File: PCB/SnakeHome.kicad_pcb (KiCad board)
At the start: 2 copper layers, 26.7 x 55.9 mm, 7 parts, among them J1 Raspberry_Pi_4, U1 Temp&Humidity_R1, U2 PIR_motion_Kitchen, U4 PIR_motion_Toilet, U5 Temp&Humidity_R2, U6 Temp&Humidity_R3, U7 Temp&Humidity_Kitchen

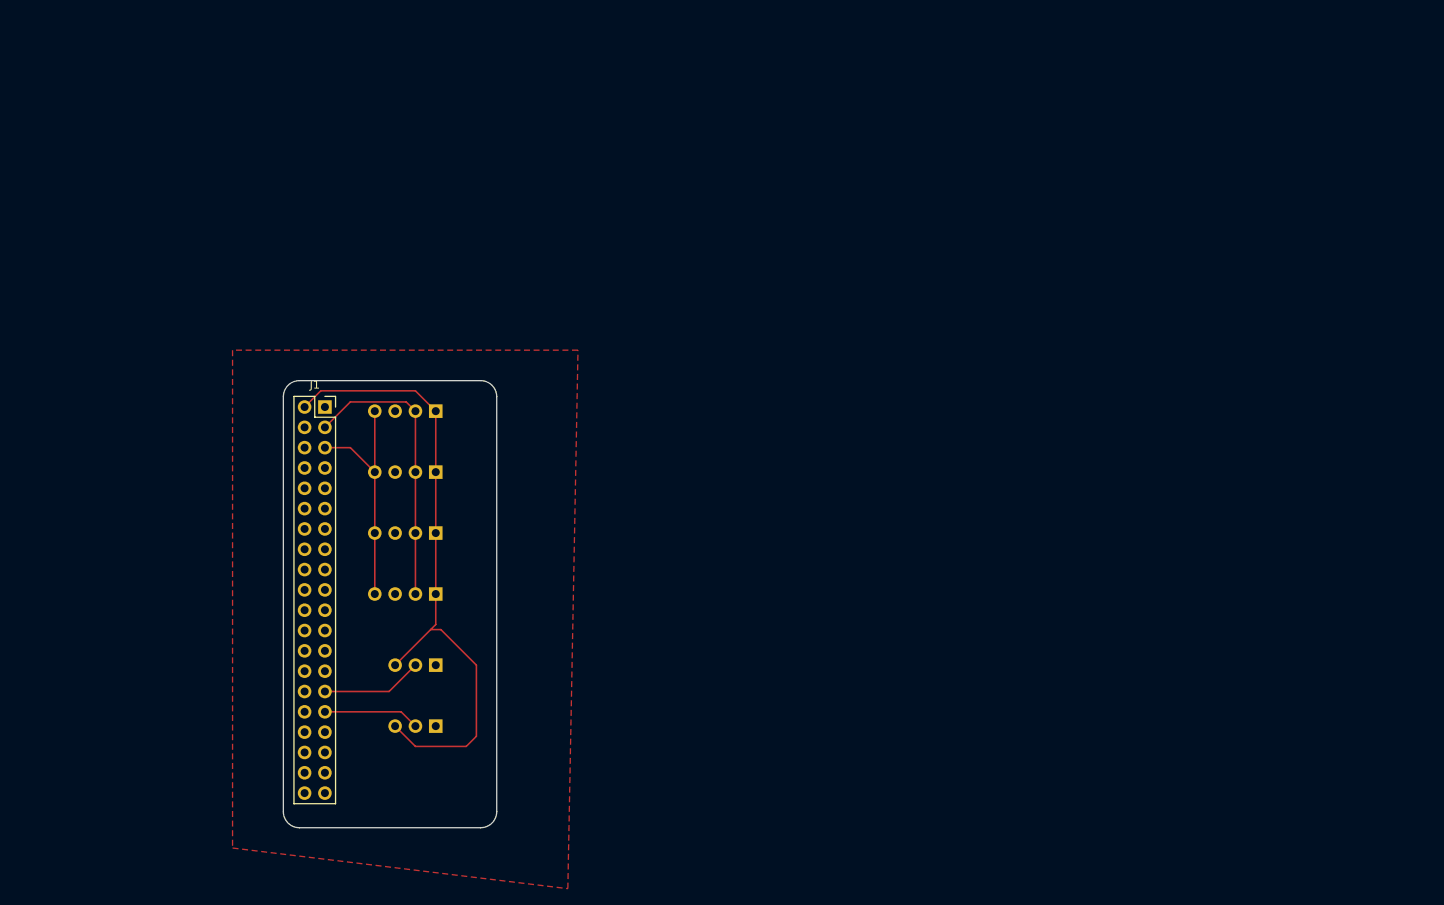
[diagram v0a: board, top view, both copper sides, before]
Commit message: choosed smd Rs and placed the components on the PCB
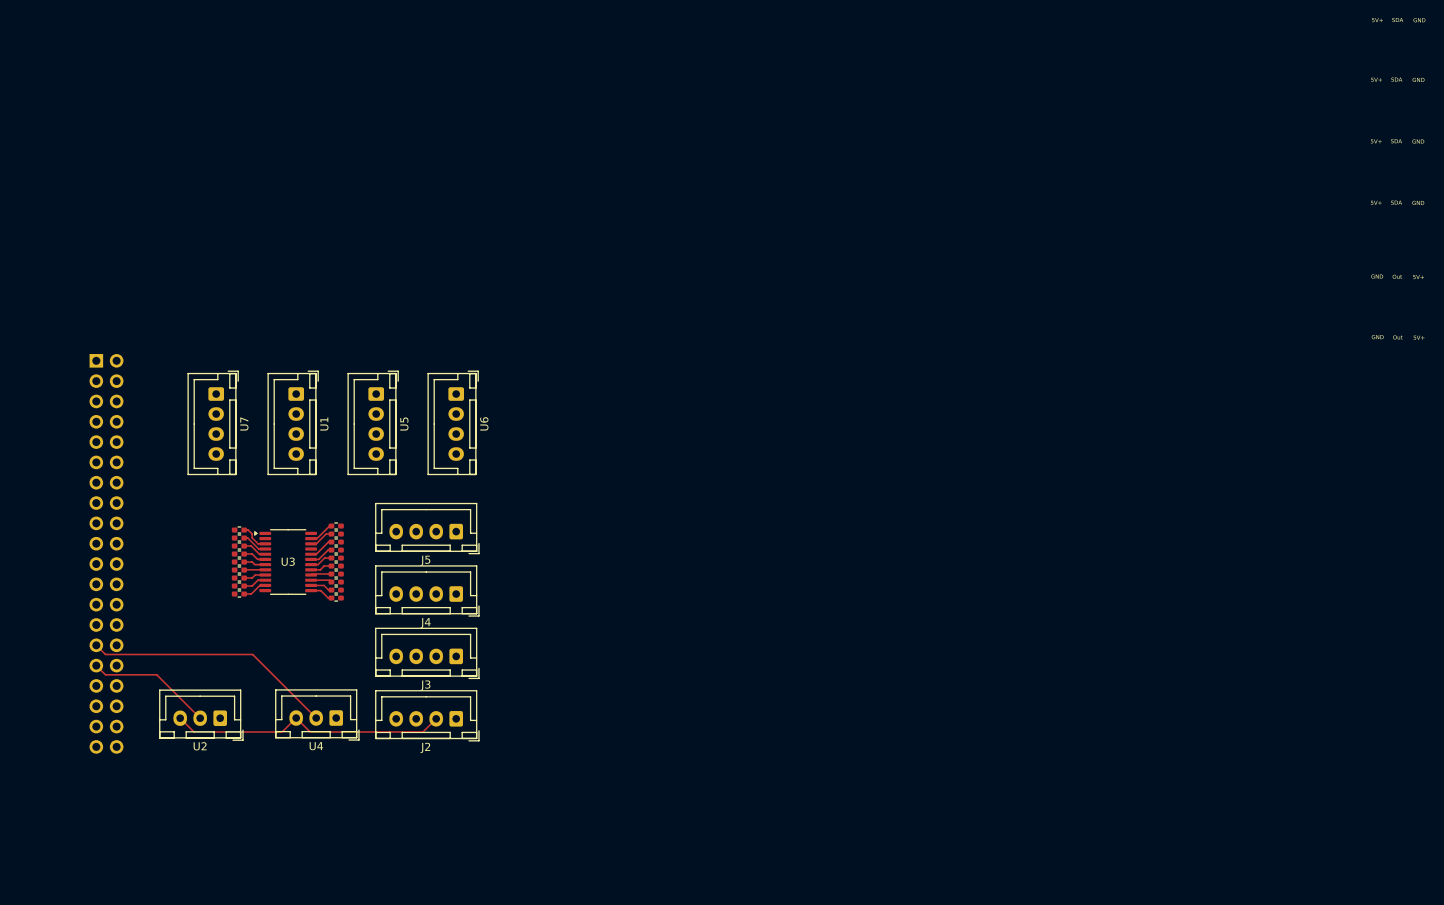
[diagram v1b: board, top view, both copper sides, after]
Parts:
- added J2: Conn_01x04_Pin, Connector_JST:JST_XH_B4B-XH-A_1x04_P2.50mm_Vertical, F.Cu at (143.5, 110.8)
- added J3: Conn_01x04_Pin, Connector_JST:JST_XH_B4B-XH-A_1x04_P2.50mm_Vertical, F.Cu at (143.5, 103.0)
- added J4: Conn_01x04_Pin, Connector_JST:JST_XH_B4B-XH-A_1x04_P2.50mm_Vertical, F.Cu at (143.5, 95.2)
- added J5: Conn_01x04_Pin, Connector_JST:JST_XH_B4B-XH-A_1x04_P2.50mm_Vertical, F.Cu at (143.5, 87.5)
- added R1: R, Resistor_SMD:R_0402_1005Metric_Pad0.72x0.64mm_HandSolder, F.Cu at (116.4, 87.2)
- added R10: R, Resistor_SMD:R_0402_1005Metric_Pad0.72x0.64mm_HandSolder, F.Cu at (128.5, 94.8)
- added R11: R, Resistor_SMD:R_0402_1005Metric_Pad0.72x0.64mm_HandSolder, F.Cu at (128.5, 90.8)
- added R12: R, Resistor_SMD:R_0402_1005Metric_Pad0.72x0.64mm_HandSolder, F.Cu at (128.5, 95.8)
- added R13: R, Resistor_SMD:R_0402_1005Metric_Pad0.72x0.64mm_HandSolder, F.Cu at (128.5, 91.8)
- added R14: R, Resistor_SMD:R_0402_1005Metric_Pad0.72x0.64mm_HandSolder, F.Cu at (128.5, 92.8)
- added R15: R, Resistor_SMD:R_0402_1005Metric_Pad0.72x0.64mm_HandSolder, F.Cu at (128.5, 88.8)
- added R16: R, Resistor_SMD:R_0402_1005Metric_Pad0.72x0.64mm_HandSolder, F.Cu at (128.5, 93.8)
- added R17: R, Resistor_SMD:R_0402_1005Metric_Pad0.72x0.64mm_HandSolder, F.Cu at (128.5, 89.8)
- added R18: R, Resistor_SMD:R_0402_1005Metric_Pad0.72x0.64mm_HandSolder, F.Cu at (128.5, 87.8)
- added R19: R, Resistor_SMD:R_0402_1005Metric_Pad0.72x0.64mm_HandSolder, F.Cu at (128.5, 86.8)
- added R2: R, Resistor_SMD:R_0402_1005Metric_Pad0.72x0.64mm_HandSolder, F.Cu at (116.4, 89.2)
- added R3: R, Resistor_SMD:R_0402_1005Metric_Pad0.72x0.64mm_HandSolder, F.Cu at (116.4, 88.2)
- added R4: R, Resistor_SMD:R_0402_1005Metric_Pad0.72x0.64mm_HandSolder, F.Cu at (116.4, 91.2)
- added R5: R, Resistor_SMD:R_0402_1005Metric_Pad0.72x0.64mm_HandSolder, F.Cu at (116.4, 90.2)
- added R6: R, Resistor_SMD:R_0402_1005Metric_Pad0.72x0.64mm_HandSolder, F.Cu at (116.4, 93.2)
- added R7: R, Resistor_SMD:R_0402_1005Metric_Pad0.72x0.64mm_HandSolder, F.Cu at (116.4, 92.2)
- added R8: R, Resistor_SMD:R_0402_1005Metric_Pad0.72x0.64mm_HandSolder, F.Cu at (116.4, 95.2)
- added R9: R, Resistor_SMD:R_0402_1005Metric_Pad0.72x0.64mm_HandSolder, F.Cu at (116.4, 94.2)
- added U3: TCA9548APWR, Package_SO:TSSOP-24_4.4x7.8mm_P0.65mm, F.Cu at (122.5, 91.2)
- J1: moved to B.Cu
- U1, U5, U6, U7: footprint Connector_PinHeader_2.54mm:PinHeader_1x04_P2.54mm_Vertical -> Connector_JST:JST_XH_B4B-XH-A_1x04_P2.50mm_Vertical; moved to F.Cu
- U2, U4: footprint Connector_PinHeader_2.54mm:PinHeader_1x03_P2.54mm_Vertical -> Connector_JST:JST_XH_B3B-XH-A_1x03_P2.50mm_Vertical; moved to F.Cu
- moved U1 30.5 mm to (123.5, 70.2), turned to -90 degrees
- moved J1 29.2 mm to (98.5, 66.1), turned to 180 degrees
- moved U7 27.5 mm to (113.5, 70.2), turned to -90 degrees
- moved U2 27.0 mm to (114.0, 110.8), turned to 180 degrees
- moved U5 18.9 mm to (133.5, 70.2), turned to -90 degrees
- moved U4 14.1 mm to (128.5, 110.8), turned to 180 degrees
- moved U6 10.1 mm to (143.5, 70.2), turned to -90 degrees
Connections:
- J1 pad 3: SDA_temp -> SDA_Bus
- J1 pad 5: SCL_temp -> SCL_Bus
- U1 pad 2: SDA_temp -> SDA_R1
- U1 pad 4: SCL_temp -> SCL_R1
- U5 pad 2: SDA_temp -> SDA_R2
- U5 pad 4: SCL_temp -> SCL_R2
- U6 pad 2: SDA_temp -> SDA_R3
- U6 pad 4: SCL_temp -> SCL_R3
- U7 pad 2: SDA_temp -> SDA_Ki
- U7 pad 4: SCL_temp -> SCL_Ki
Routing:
- net +5V: track 80.3 -> 34.8 mm
- net SDA_temp: track 36.0 -> 0.00 mm
- net SCL_temp: track 30.4 -> 0.00 mm
- net motion_out2: track 12.7 -> 31.3 mm
- net motion_out: track 12.1 -> 15.7 mm
- net Net-(U3-~{RESET}): track 0.00 -> 3.64 mm
- net SCL_R1: track 0.00 -> 3.21 mm
- net SDA_Bus: track 0.00 -> 3.19 mm
- net SDA_4: track 0.00 -> 3.17 mm
- net SDA_Ki: track 0.00 -> 3.08 mm
- net SDA_R1: track 0.00 -> 3.06 mm
- net SCL_Bus: track 0.00 -> 3.05 mm
- net SCL_4: track 0.00 -> 3.03 mm
- net SCL_Ki: track 0.00 -> 2.94 mm
- net SCL_1: track 0.00 -> 2.92 mm
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- removed copper zone on F.Cu, net GND
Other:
- board outline removed
- board text removed: "SCL"

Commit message: Traced all the Components, used two back layer traces 😭
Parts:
- moved U6 30.0 mm to (113.5, 70.2)
- moved J2 15.6 mm to (143.5, 95.2)
- moved J4 15.6 mm to (143.5, 110.8)
- moved U1 10.0 mm to (133.5, 70.2)
- moved U5 10.0 mm to (143.5, 70.2)
- moved U7 10.0 mm to (123.5, 70.2)
- moved R10 0.25 mm to (128.5, 94.5)
- moved R11 0.25 mm to (128.5, 90.5)
- moved R12 0.25 mm to (128.5, 95.5)
- moved R13 0.25 mm to (128.5, 91.5)
- moved R14 0.25 mm to (128.5, 92.5)
- moved R15 0.25 mm to (128.5, 88.5)
- moved R16 0.25 mm to (128.5, 93.5)
- moved R17 0.25 mm to (128.5, 89.5)
- moved R18 0.25 mm to (128.5, 87.5)
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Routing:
- net +5V: track 34.8 -> 238.1 mm
- net SCL_Bus: track 3.05 -> 92.6 mm
- net SDA_Bus: track 3.19 -> 91.8 mm
- net SCL_Ki: track 2.94 -> 55.8 mm
- net SCL_R2: track 2.92 -> 45.2 mm
- net SDA_R3: track 2.79 -> 42.6 mm
- net SCL_R3: track 2.65 -> 37.8 mm
- net SDA_R2: track 2.77 -> 36.2 mm
- net SDA_Ki: track 3.08 -> 33.3 mm
- net SDA_R1: track 3.06 -> 32.1 mm
- net SCL_3: track 2.74 -> 30.3 mm
- net SDA_3: track 2.88 -> 29.7 mm
- net SCL_4: track 3.03 -> 29.4 mm, vias 0 -> 1
- net SDA_4: track 3.17 -> 25.4 mm, vias 0 -> 1
- net SCL_2: track 2.63 -> 24.0 mm
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
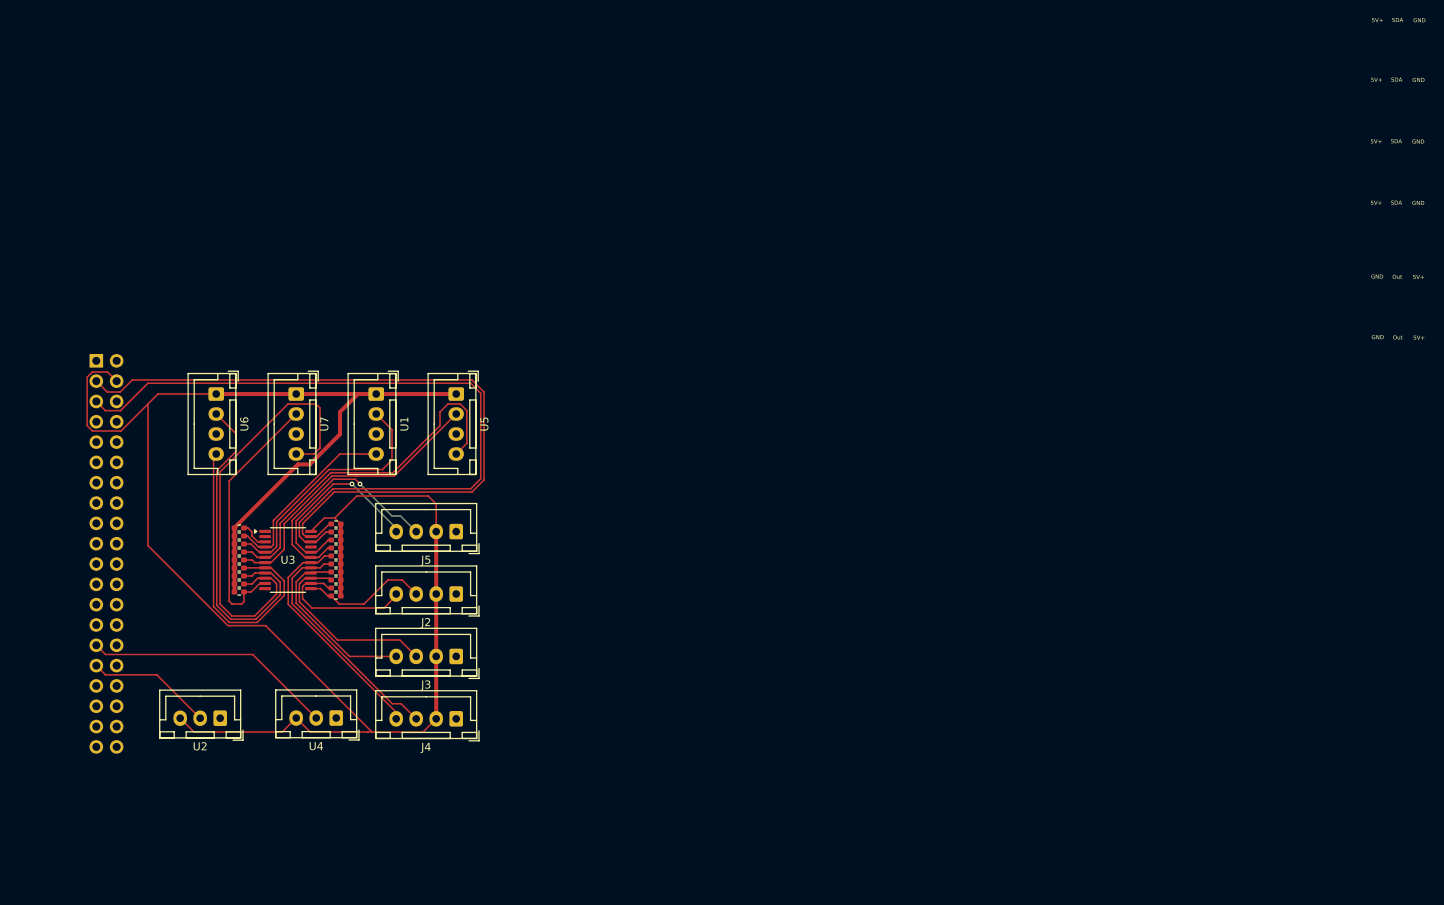
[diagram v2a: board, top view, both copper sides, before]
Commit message: Made GND fill zones and fixed missed ones
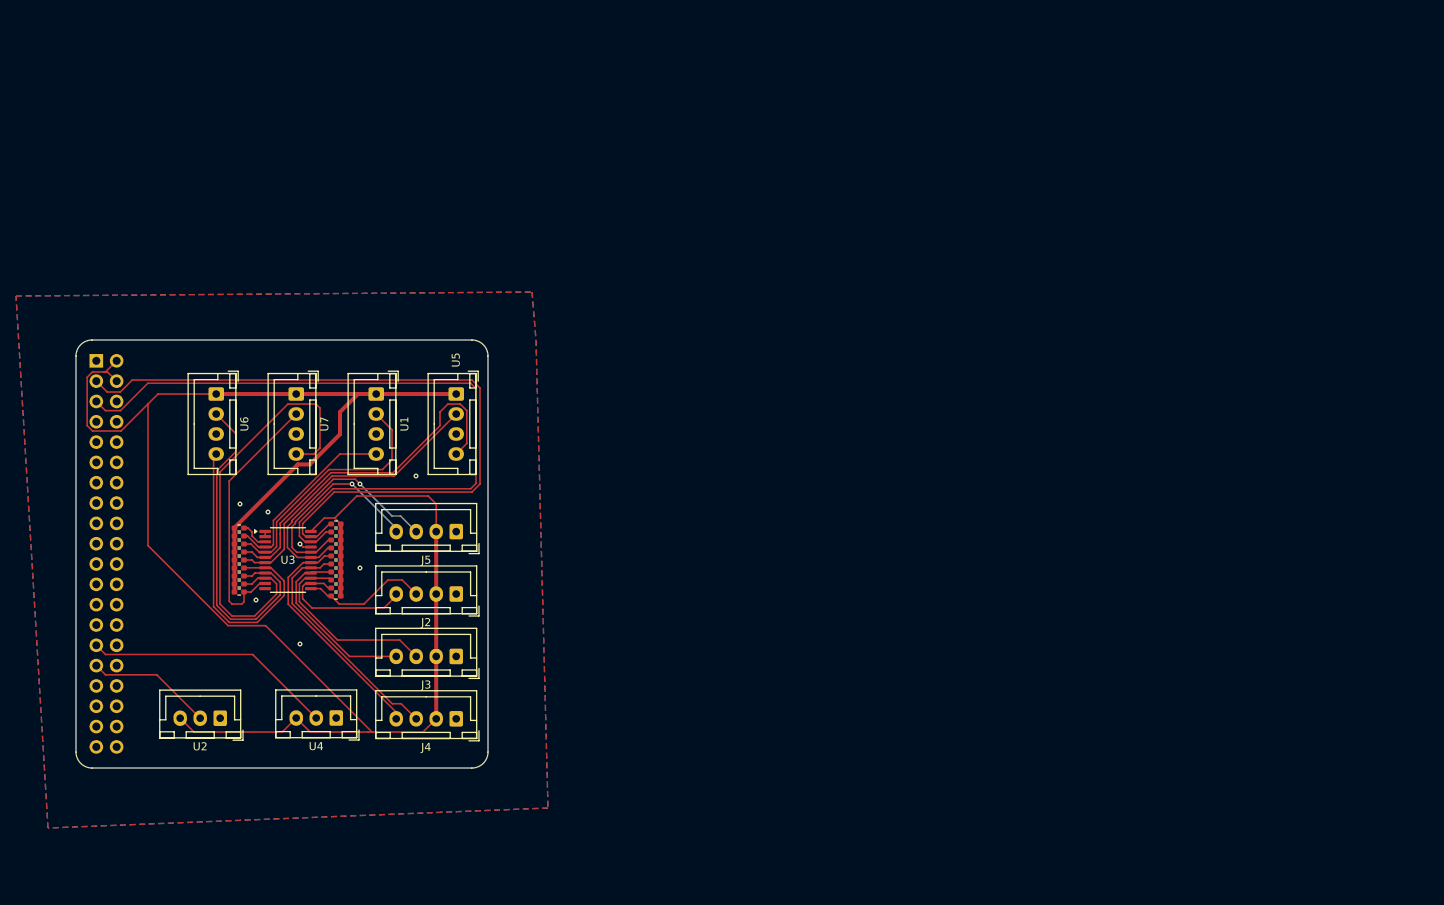
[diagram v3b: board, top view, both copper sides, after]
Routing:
- net GND: track 0.00 -> 2.17 mm, vias 0 -> 7
- net +5V: track 238.1 -> 240.3 mm
- net SDA_4: track 25.4 -> 26.4 mm
- net SCL_4: track 29.4 -> 30.5 mm
- added copper zone on B.Cu, net GND
- added copper zone on F.Cu, net GND
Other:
- board outline added: 51.5 x 53.5 mm
- board text removed: "5V+"
- board text removed: "GND"
- board text removed: "Out"
- board text removed: "SDA"
